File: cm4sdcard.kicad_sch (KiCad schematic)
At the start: 5 parts, among them J5 MEM2067-02-180-00-A_REVB, U13 LM3525M-H_NPOB

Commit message: board refresh
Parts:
- renumbered C24 to C22, C25 to C23, R41 to R44, U13 to U12
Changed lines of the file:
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@@
   (symbol (lib_id "power:GND") (at 178.435 128.27 0) (unit 1)
     (in_bom yes) (on_board yes)
-    (property "Reference" "#PWR038" (id 0) (at 178.435 134.62 0)
+    (property "Reference" "#PWR036" (id 0) (at 178.435 134.62 0)
       (effects (font (size 1.27 1.27)) hide)
     )
@@
   (symbol (lib_id "Device:R_Small") (at 104.14 66.04 90) (unit 1)
     (in_bom yes) (on_board yes) (fields_autoplaced)
-    (property "Reference" "R41" (id 0) (at 104.14 60.96 90))
+    (property "Reference" "R44" (id 0) (at 104.14 60.96 90))
     (property "Value" "12k 1%" (id 1) (at 104.14 63.5 90))
     (property "Footprint" "Resistor_SMD:R_0402_1005Metric" (id 2) (at 104.14 66.04 0)
@@
   (symbol (lib_id "Device:C_Small") (at 127 71.12 90) (unit 1)
     (in_bom yes) (on_board yes)
-    (property "Reference" "C24" (id 0) (at 125.73 69.85 90)
+    (property "Reference" "C22" (id 0) (at 125.73 69.85 90)
       (effects (font (size 1.27 1.27)) (justify left))
     )
@@
   (symbol (lib_id "power:GND") (at 167.64 83.82 0) (unit 1)
     (in_bom yes) (on_board yes)
-    (property "Reference" "#PWR037" (id 0) (at 167.64 90.17 0)
+    (property "Reference" "#PWR035" (id 0) (at 167.64 90.17 0)
       (effects (font (size 1.27 1.27)) hide)
     )
@@
   (symbol (lib_id "power:GND") (at 134.62 83.82 0) (unit 1)
     (in_bom yes) (on_board yes)
-    (property "Reference" "#PWR036" (id 0) (at 134.62 90.17 0)
+    (property "Reference" "#PWR034" (id 0) (at 134.62 90.17 0)
       (effects (font (size 1.27 1.27)) hide)
     )
@@
   (symbol (lib_id "Power_Protection_TI:LM3525M-H_NPOB") (at 144.78 68.58 0) (unit 1)
     (in_bom yes) (on_board yes)
-    (property "Reference" "U13" (id 0) (at 139.7 62.23 0))
+    (property "Reference" "U12" (id 0) (at 139.7 62.23 0))
     (property "Value" "LM3525M-H_NPOB" (id 1) (at 144.78 78.105 0))
     (property "Footprint" "Package_SO_MyOwn:SOIC-8_3.9x4.9mm_P1.27mm" (id 2) (at 145.034 86.106 0)
@@
   (symbol (lib_id "Device:C_Small") (at 167.64 74.93 0) (mirror x) (unit 1)
     (in_bom yes) (on_board yes)
-    (property "Reference" "C25" (id 0) (at 169.545 74.295 0)
+    (property "Reference" "C23" (id 0) (at 169.545 74.295 0)
       (effects (font (size 1.27 1.27)) (justify left))
     )

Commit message: work on control logic
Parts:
- renumbered R44 to R46
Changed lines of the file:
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@@
   (symbol (lib_id "Device:R_Small") (at 104.14 66.04 90) (unit 1)
     (in_bom yes) (on_board yes) (fields_autoplaced)
-    (property "Reference" "R44" (id 0) (at 104.14 60.96 90))
+    (property "Reference" "R46" (id 0) (at 104.14 60.96 90))
     (property "Value" "12k 1%" (id 1) (at 104.14 63.5 90))
     (property "Footprint" "Resistor_SMD:R_0402_1005Metric" (id 2) (at 104.14 66.04 0)

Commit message: work on control logic
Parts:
- renumbered C22 to C24, C23 to C25, R46 to R49, U12 to U13
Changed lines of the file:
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@@
   (symbol (lib_id "power:GND") (at 178.435 128.27 0) (unit 1)
     (in_bom yes) (on_board yes)
-    (property "Reference" "#PWR036" (id 0) (at 178.435 134.62 0)
+    (property "Reference" "#PWR037" (id 0) (at 178.435 134.62 0)
       (effects (font (size 1.27 1.27)) hide)
     )
@@
   (symbol (lib_id "Device:R_Small") (at 104.14 66.04 90) (unit 1)
     (in_bom yes) (on_board yes) (fields_autoplaced)
-    (property "Reference" "R46" (id 0) (at 104.14 60.96 90))
+    (property "Reference" "R49" (id 0) (at 104.14 60.96 90))
     (property "Value" "12k 1%" (id 1) (at 104.14 63.5 90))
     (property "Footprint" "Resistor_SMD:R_0402_1005Metric" (id 2) (at 104.14 66.04 0)
@@
   (symbol (lib_id "Device:C_Small") (at 127 71.12 90) (unit 1)
     (in_bom yes) (on_board yes)
-    (property "Reference" "C22" (id 0) (at 125.73 69.85 90)
+    (property "Reference" "C24" (id 0) (at 125.73 69.85 90)
       (effects (font (size 1.27 1.27)) (justify left))
     )
@@
   (symbol (lib_id "power:GND") (at 167.64 83.82 0) (unit 1)
     (in_bom yes) (on_board yes)
-    (property "Reference" "#PWR035" (id 0) (at 167.64 90.17 0)
+    (property "Reference" "#PWR036" (id 0) (at 167.64 90.17 0)
       (effects (font (size 1.27 1.27)) hide)
     )
@@
   (symbol (lib_id "power:GND") (at 134.62 83.82 0) (unit 1)
     (in_bom yes) (on_board yes)
-    (property "Reference" "#PWR034" (id 0) (at 134.62 90.17 0)
+    (property "Reference" "#PWR035" (id 0) (at 134.62 90.17 0)
       (effects (font (size 1.27 1.27)) hide)
     )
@@
   (symbol (lib_id "Power_Protection_TI:LM3525M-H_NPOB") (at 144.78 68.58 0) (unit 1)
     (in_bom yes) (on_board yes)
-    (property "Reference" "U12" (id 0) (at 139.7 62.23 0))
+    (property "Reference" "U13" (id 0) (at 139.7 62.23 0))
     (property "Value" "LM3525M-H_NPOB" (id 1) (at 144.78 78.105 0))
     (property "Footprint" "Package_SO_MyOwn:SOIC-8_3.9x4.9mm_P1.27mm" (id 2) (at 145.034 86.106 0)
@@
   (symbol (lib_id "Device:C_Small") (at 167.64 74.93 0) (mirror x) (unit 1)
     (in_bom yes) (on_board yes)
-    (property "Reference" "C23" (id 0) (at 169.545 74.295 0)
+    (property "Reference" "C25" (id 0) (at 169.545 74.295 0)
       (effects (font (size 1.27 1.27)) (justify left))
     )

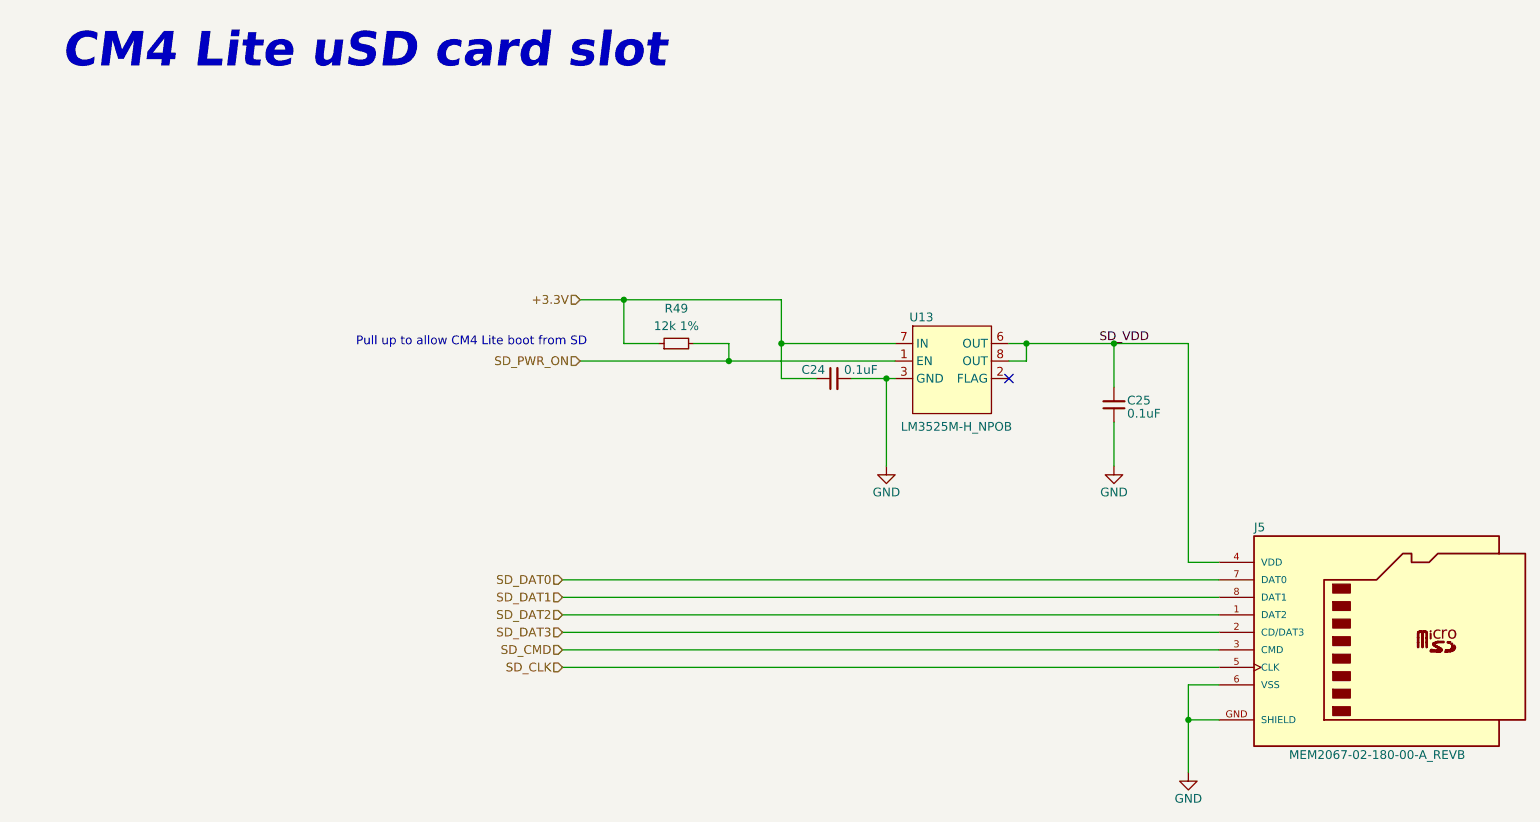
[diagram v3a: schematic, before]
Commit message: connecterized faceplate, refreshed schematic
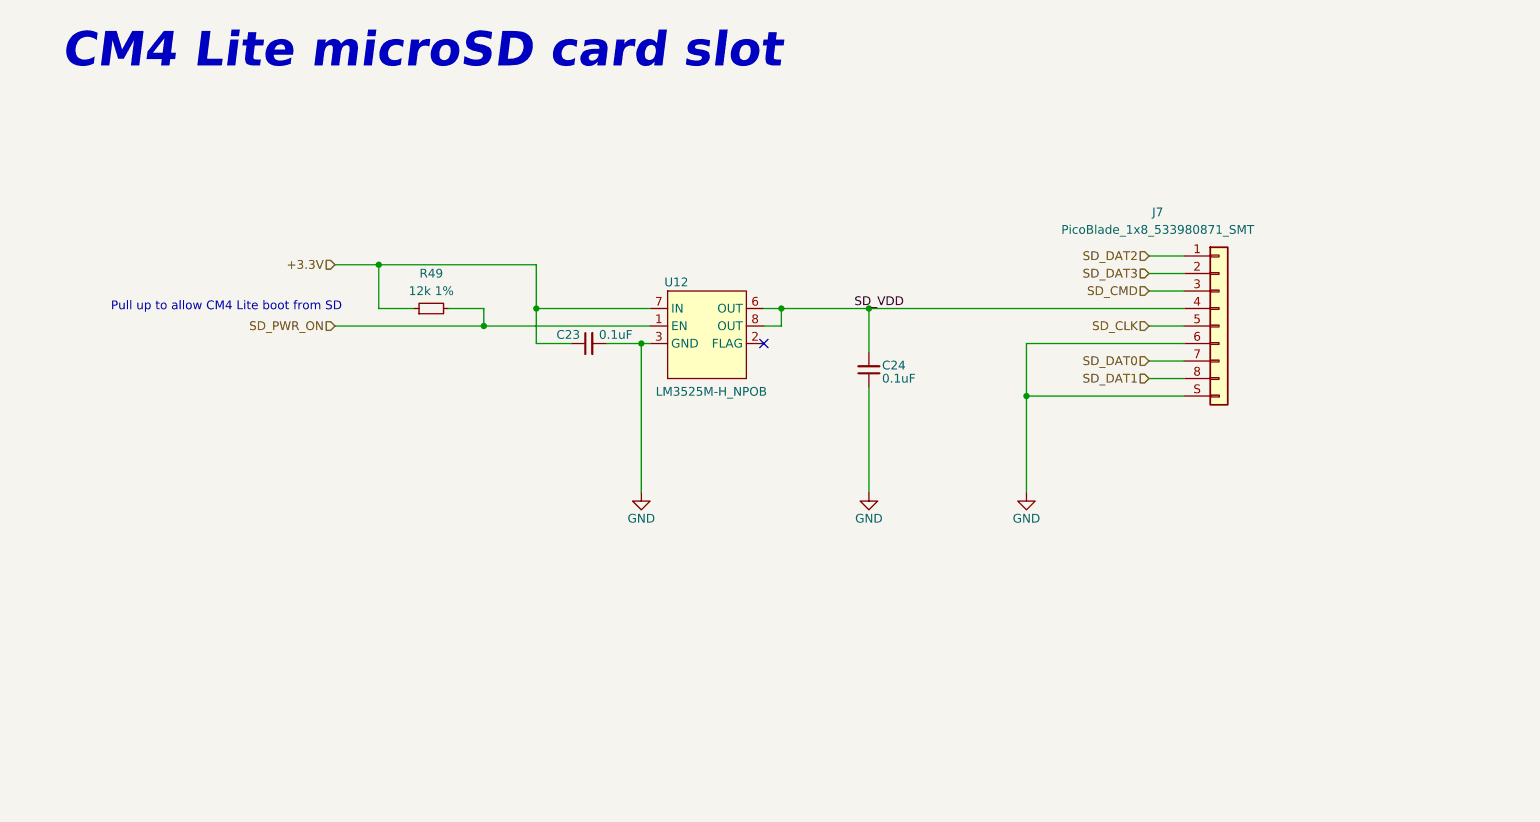
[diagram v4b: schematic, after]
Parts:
- removed J5: MEM2067-02-180-00-A_REVB, Connector_SD_GCT:GCT_MEM2067-02-180-00-A_REVB, symbol Connector_SD_GCT:MEM2067-02-180-00-A_REVB
- added J7: PicoBlade_1x8_533980871_SMT, Connector_PicoBlade_Molex:MOLEX_533980871, symbol Connector_PicoBlade_Molex:PicoBlade_1x8_533980871_SMT
- renumbered C24 to C23, C25 to C24, U13 to U12
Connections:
- net GND: now also J7.6 (Pin_6), J7.S (SHIELD)
- net SD_CLK: now also J7.5 (Pin_5)
- net SD_CMD: now also J7.3 (Pin_3)
- net SD_DAT0: now also J7.7 (Pin_7)
- net SD_DAT1: now also J7.8 (Pin_8)
- net SD_DAT2: now also J7.1 (Pin_1)
- net SD_DAT3: now also J7.2 (Pin_2)
- net SD_VDD: now also J7.4 (Pin_4)
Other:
- note added: "CM4 Lite microSD card slot"
- note removed: "CM4 Lite uSD card slot"
- title: uSD slot for CM4 Lites -> microSD slot for CM4 Lites
- moved on the sheet: C23, C24, R49, U12

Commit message: refresh
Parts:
- removed J7: PicoBlade_1x8_533980871_SMT, Connector_PicoBlade_Molex:MOLEX_533980871, symbol Connector_PicoBlade_Molex:PicoBlade_1x8_533980871_SMT
- added J7: MEM2067-02-180-00-A_REVB, Connector_SD_GCT:GCT_MEM2067-02-180-00-A_REVB, symbol Connector_SD_GCT:MEM2067-02-180-00-A_REVB
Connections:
- net GND: now also J7.6 (VSS), J7.GND (SHIELD)
- net SD_CLK: now also J7.5 (CLK)
- net SD_CMD: now also J7.3 (CMD)
- net SD_DAT0: now also J7.7 (DAT0)
- net SD_DAT1: now also J7.8 (DAT1)
- net SD_DAT2: now also J7.1 (DAT2)
- net SD_DAT3: now also J7.2 (CD/DAT3)
- net SD_VDD: now also J7.4 (VDD)
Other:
- moved on the sheet: C23, C24, R49, U12
